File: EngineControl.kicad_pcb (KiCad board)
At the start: 4 copper layers, 70 x 70 mm, 47 parts, among them J1 Debugger, J2 Centroid, J3 BATT, J5 UART, J7 GPIO, Q1 Q_NMOS_GSD, Q2 Q_NMOS_GSD, SW1 BOOT, U1 STM32F103C8Tx, U2 SN65HVD230, U3 AMS1117-3.3, U4 CPC1135N, Y1 8 Mhz 5032

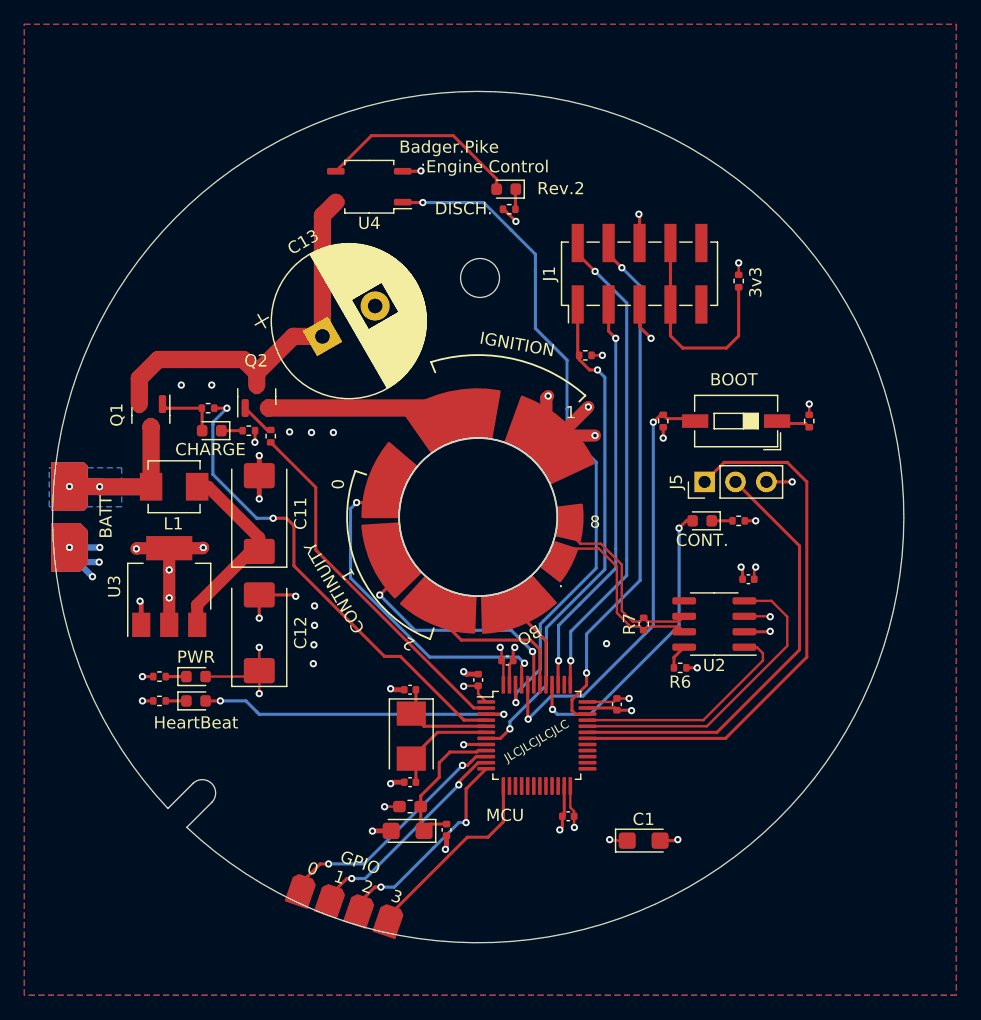
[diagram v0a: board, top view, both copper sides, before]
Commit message: Apply schematic updates to PCB
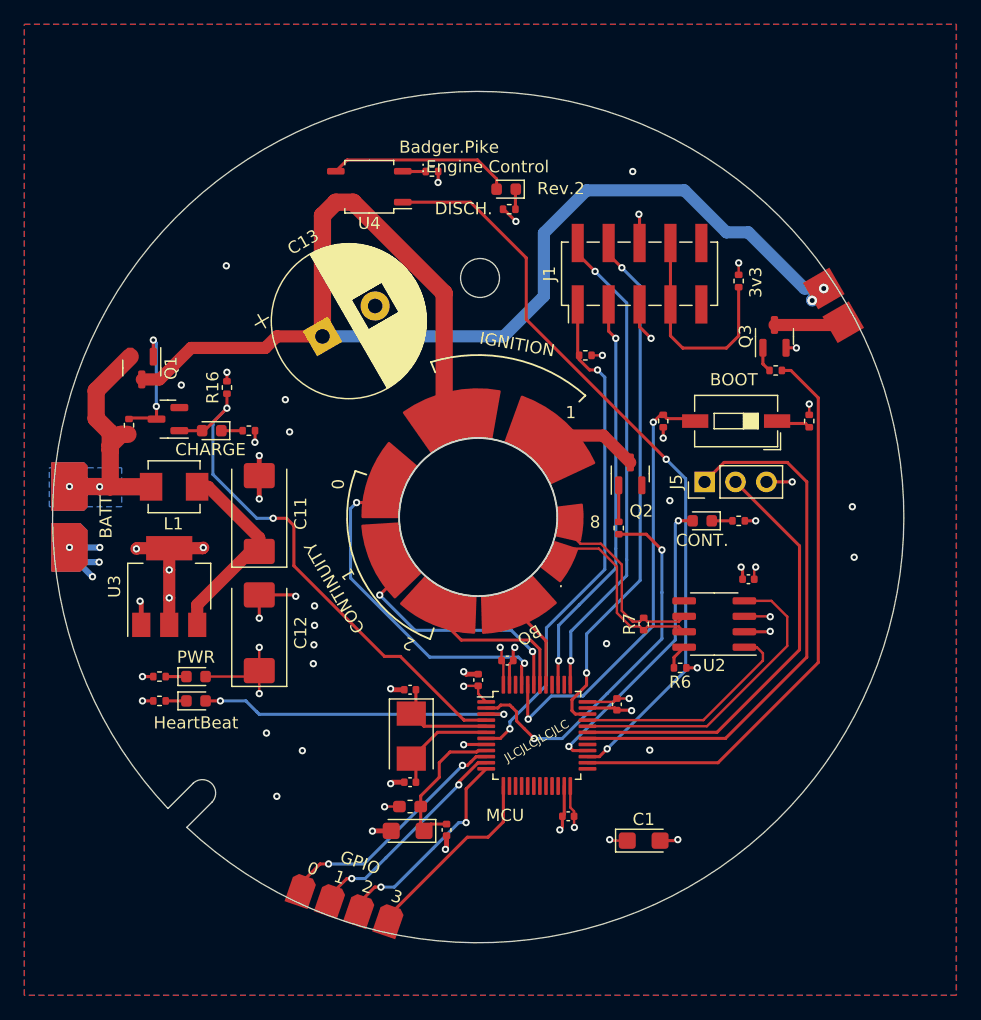
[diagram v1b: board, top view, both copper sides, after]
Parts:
- added J4: PYRO1, Connector_PinHeader_2.54mm:PinHeader_1x02_P2.54mm_Vertical_SMD_Pin1Left, F.Cu at (129.2, 82.6)
- added Q3: Q_NMOS_GSD, Package_TO_SOT_SMD:SOT-23, F.Cu at (124.3, 85.2)
- added Q4: Q_NMOS_GSD, Package_TO_SOT_SMD:SOT-23, F.Cu at (74.5, 92.0)
- added R14: 1.5k, Resistor_SMD:R_0402_1005Metric, F.Cu at (96.2, 71.6)
- added R15: 220R, Resistor_SMD:R_0402_1005Metric, F.Cu at (124.5, 88.0)
- added R16: 10k, Resistor_SMD:R_0402_1005Metric, F.Cu at (79.3, 89.4)
- Q1: value Q_NMOS_GSD -> PMOS-GSD
- R11: value 220R -> 100k
- R9: value 1.5k -> 220
- moved Q2 31.3 mm to (112.5, 96.5)
- moved R13 29.6 mm to (111.5, 100.9)
- moved R11 6.65 mm to (71.3, 92.5), turned to -90 degrees
- moved Q1 3.97 mm to (72.3, 87.8)
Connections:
- C13 pad 1: Net-(C13-Pad1) -> /Ignition/IGN+
- D4 pad 2: Net-(D4-Pad2) -> /Ignition/CHARGE
- J2 pad 1: GND -> /Ignition/IGN-
- Q1 pad 1: Net-(D4-Pad2) -> Net-(Q1-Pad1)
- Q1 pad 2: Net-(C13-Pad1) -> /Ignition/BATT+
- Q1 pad 3: /Ignition/BATT+ -> /Ignition/IGN+
- Q2 pad 2: /Ignition/IGN+ -> GND
- Q2 pad 3: Net-(C13-Pad1) -> /Ignition/IGN-
- R11 pad 1: /Ignition/CHARGE -> Net-(Q1-Pad1)
- R11 pad 2: Net-(D4-Pad2) -> /Ignition/BATT+
- U1 pad 26: unconnected-(U1-Pad26) -> /Ignition/IGN1
- U1 pad 27: unconnected-(U1-Pad27) -> /Ignition/nDISCHARGE
- U1 pad 28: unconnected-(U1-Pad28) -> /Ignition/CONT_INDICATION
- U1 pad 40: /Ignition/CONT_INDICATION -> unconnected-(U1-Pad40)
- U1 pad 46: /Ignition/nDISCHARGE -> unconnected-(U1-Pad46)
- U4 pad 2: GND -> Net-(U4-Pad2)
- U4 pad 4: Net-(C13-Pad1) -> /Ignition/IGN+
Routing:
- net /Ignition/IGN+: track 15.6 -> 104.3 mm, vias 0 -> 2
- net /Ignition/IGN1: track 0.00 -> 48.1 mm
- net Net-(C13-Pad1): track 32.0 -> 0.00 mm
- net GND: track 71.4 -> 59.8 mm, vias 45 -> 51
- net Net-(Q1-Pad1): track 0.00 -> 10.3 mm, vias 0 -> 2
- net /Ignition/BATT+: track 11.6 -> 21.5 mm
- net /Ignition/IGN-: track 0.00 -> 8.02 mm
- net /Ignition/nDISCHARGE: track 55.8 -> 62.4 mm
- net /Ignition/PYRO1-: track 0.00 -> 5.74 mm
- net Net-(D4-Pad2): track 5.24 -> 0.00 mm
- net /Ignition/CHARGE: track 39.7 -> 44.5 mm
- net Net-(Q3-Pad1): track 0.00 -> 2.09 mm
- net Net-(U4-Pad2): track 0.00 -> 1.90 mm
- net Net-(D5-Pad2): track 16.7 -> 15.1 mm
- net /Ignition/IGN0: track 29.8 -> 30.9 mm, vias 0 -> 2

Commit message: Bump to Rev.3
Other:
- board text added: "Rev.3"
- board text removed: "Rev.2"
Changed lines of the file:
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@@
     (effects (font (size 1 1) (thickness 0.15)))
   )
-  (gr_text "Rev.2" (at 106.8 73.01) (layer "F.SilkS")
+  (gr_text "Rev.3" (at 106.8 73.01) (layer "F.SilkS")
     (effects (font (size 1 1) (thickness 0.15)))
   )

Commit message: Bump version to Rev4 for next release
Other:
- board text added: "PYRO1"
- board text added: "Rev.4"
- board text removed: "Rev.3"
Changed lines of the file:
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@@
+    (effects (font (size 1 1) (thickness 0.15)))
+  )
+  (gr_text "PYRO1" (at 126.85 83.96 120) (layer "F.SilkS")
     (effects (font (size 1 1) (thickness 0.15)))
   )
@@
     (effects (font (size 1 1) (thickness 0.15)))
   )
-  (gr_text "Rev.3" (at 106.8 73.01) (layer "F.SilkS")
+  (gr_text "Rev.4" (at 106.8 73.01) (layer "F.SilkS")
     (effects (font (size 1 1) (thickness 0.15)))
   )

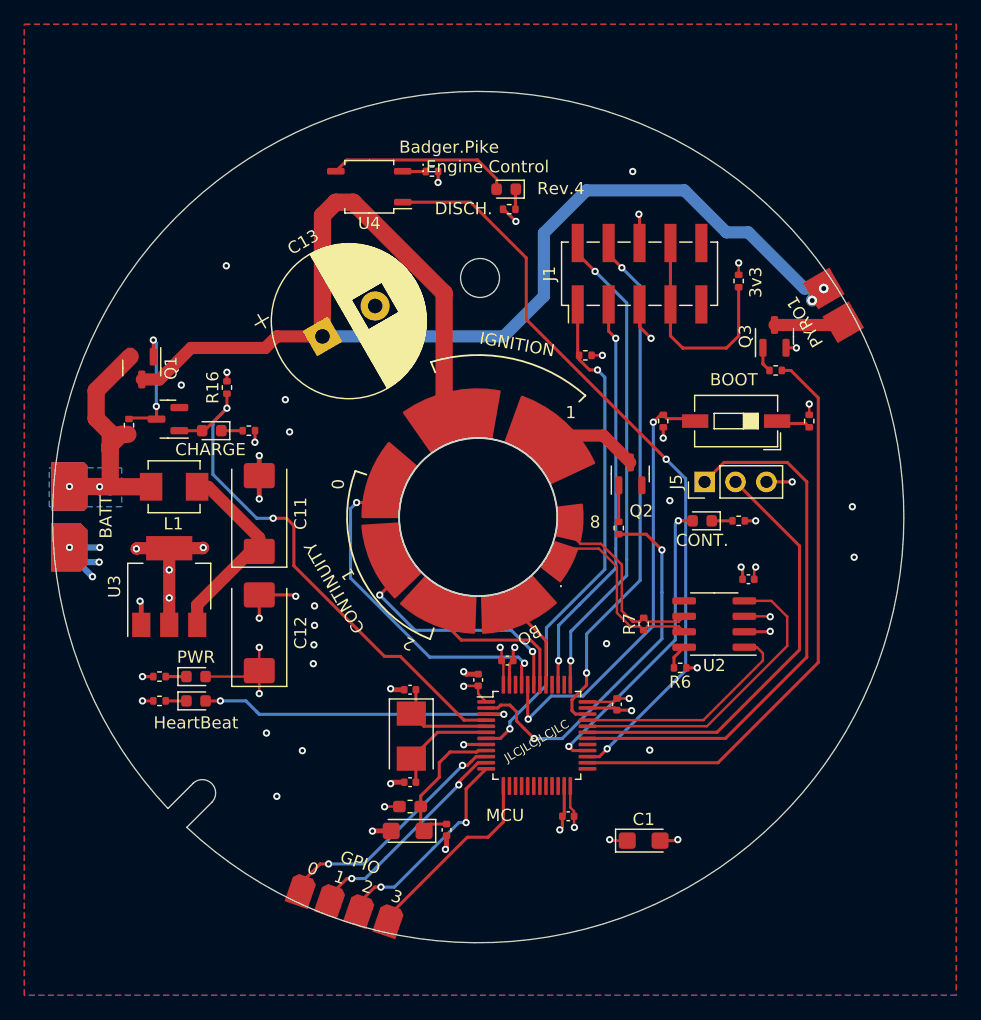
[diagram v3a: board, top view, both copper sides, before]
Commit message: Add pressure sensor schema and pcb layout for pyro and reverse polarity
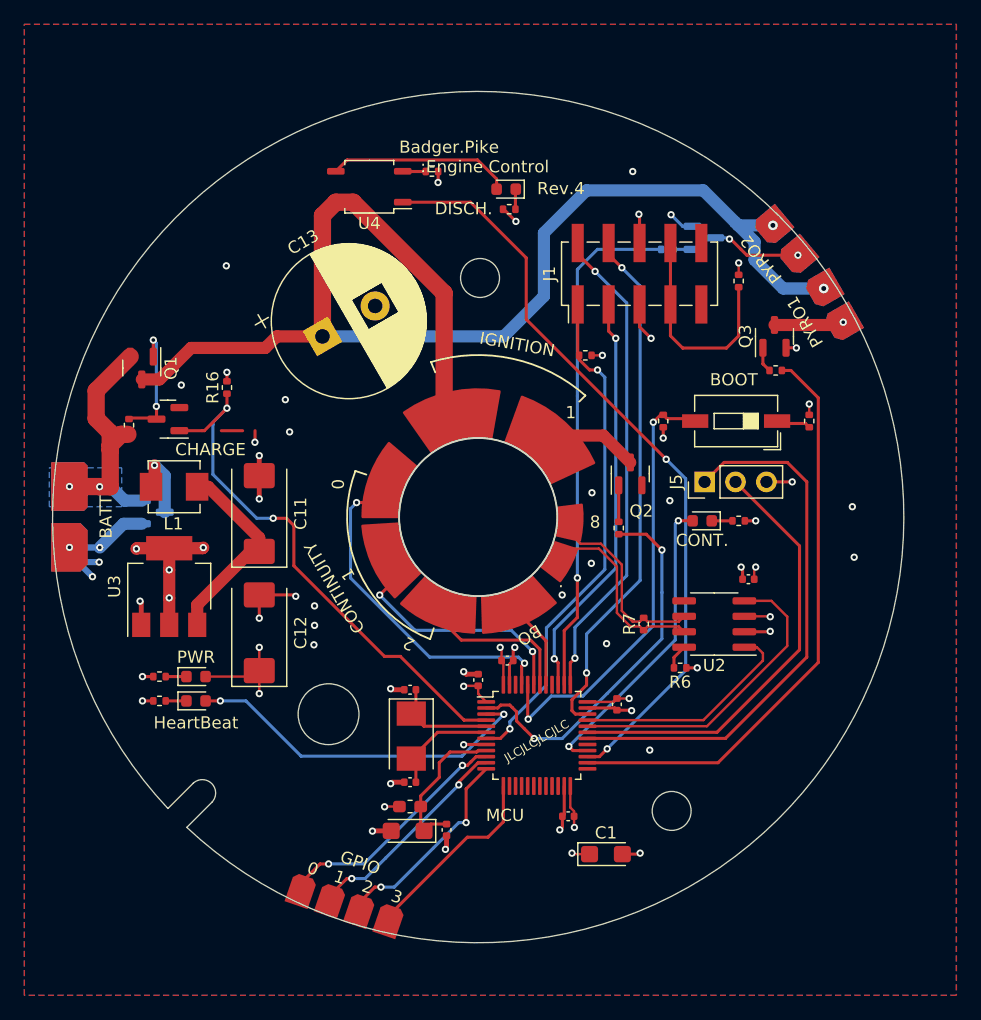
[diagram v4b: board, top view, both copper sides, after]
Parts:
- removed D4: LED_Charge, LED_SMD:LED_0603_1608Metric
- added J6: PYRO2, Connector_PinHeader_2.54mm:PinHeader_1x02_P2.54mm_Vertical_SMD_Pin1Left, F.Cu at (125.2, 77.3)
- added Q5: PMOS-GSD, Package_TO_SOT_SMD:SOT-23, B.Cu at (73.3, 99.6)
- added Q6: Q_NMOS_GSD, Package_TO_SOT_SMD:SOT-23, B.Cu at (118.5, 77.1)
- added REF**: MountingHole_5mm, MountingHole:MountingHole_5mm, F.Cu at (87.7, 116.2)
- added REF**: MountingHole_3.2mm_M3, MountingHole:MountingHole_3.2mm_M3, F.Cu at (115.9, 124.2)
- C12: value 100u -> 100uF
- R9: value 220 -> 220R; moved to B.Cu
- moved R9 37.5 mm to (115.5, 78.0), turned to 0 degrees
- moved C1 3.29 mm to (110.5, 127.7)
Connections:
- J1 pad 10: unconnected-(J1-Pad10) -> (no net)
- J1 pad 9: unconnected-(J1-Pad9) -> (no net)
- L1 pad 1: /Ignition/BATT+ -> Net-(L1-Pad1)
- R9 pad 1: GND -> /Ignition/IGN2
- U1 pad 14: unconnected-(U1-Pad14) -> (no net)
- U1 pad 15: unconnected-(U1-Pad15) -> (no net)
- U1 pad 16: unconnected-(U1-Pad16) -> (no net)
- U1 pad 17: unconnected-(U1-Pad17) -> (no net)
- U1 pad 18: unconnected-(U1-Pad18) -> (no net)
- U1 pad 19: unconnected-(U1-Pad19) -> (no net)
- U1 pad 20: unconnected-(U1-Pad20) -> (no net)
- U1 pad 21: /MCU/SCL -> (no net)
- U1 pad 22: /MCU/SDA -> (no net)
- U1 pad 25: unconnected-(U1-Pad25) -> (no net)
- U1 pad 29: unconnected-(U1-Pad29) -> (no net)
- U1 pad 38: unconnected-(U1-Pad38) -> /Ignition/IGN2
- U1 pad 40: unconnected-(U1-Pad40) -> (no net)
- U1 pad 46: unconnected-(U1-Pad46) -> (no net)
- U2 pad 5: unconnected-(U2-Pad5) -> (no net)
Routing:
- net /Ignition/IGN2: track 0.00 -> 42.1 mm, vias 0 -> 1
- net /Ignition/PYRO2-: track 0.00 -> 7.38 mm, vias 0 -> 2
- net GND: track 59.8 -> 66.2 mm
- net Net-(L1-Pad1): track 0.00 -> 6.07 mm, vias 0 -> 1
- net Net-(D1-Pad2): track 26.4 -> 29.3 mm
- net /Ignition/IGN+: track 104.3 -> 107.0 mm
- net (no net): track 0.00 -> 1.75 mm
- net /Ignition/BATT+: track 21.5 -> 22.0 mm
- net /Ignition/PYRO1-: vias 0 -> 1
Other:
- board text added: "PYRO2"

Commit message: Finish pcb layout for rev4
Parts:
- removed the REF** at (115.9, 124.2)
- added C14: 10uF, Capacitor_Tantalum_SMD:CP_EIA-3216-18_Kemet-A, B.Cu at (122.5, 121.2)
- added C15: 100nF, Capacitor_SMD:C_0402_1005Metric, B.Cu at (120.7, 120.4)
- added C16: 100nF, Capacitor_SMD:C_0402_1005Metric, B.Cu at (120.8, 123.3)
- added R17: 10k, Resistor_SMD:R_0402_1005Metric, F.Cu at (109.2, 122.5)
- added R18: 10k, Resistor_SMD:R_0402_1005Metric, F.Cu at (106.2, 126.8)
- added U5: MPL3115A2, Package_LGA:NXP_LGA-8_3x5mm_P1.25mm_H1.1mm, B.Cu at (116.5, 121.8)
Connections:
- U1 pad 14: (no net) -> /MCU/MPL_INT1
- U1 pad 15: (no net) -> /MCU/MPL_INT2
- U1 pad 21: (no net) -> /MCU/SCL
- U1 pad 22: (no net) -> /MCU/SDA
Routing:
- net /MCU/SCL: track 0.00 -> 16.2 mm, vias 0 -> 1
- net /MCU/MPL_INT1: track 0.00 -> 15.1 mm, vias 0 -> 1
- net /MCU/MPL_INT2: track 0.00 -> 13.8 mm, vias 0 -> 1
- net /MCU/SDA: track 0.00 -> 13.0 mm, vias 0 -> 1
- net +3V3: track 42.0 -> 52.1 mm, vias 17 -> 21
- net Net-(C16-Pad1): track 0.00 -> 3.80 mm
- net GND: track 66.2 -> 69.4 mm, vias 51 -> 53
- net (no net): track 1.75 -> 0.00 mm
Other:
- board text added: "+"
- board text added: "BATT"
- board text removed: "CHARGE"

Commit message: Generate gerber file
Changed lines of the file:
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@@
     (fp_line (start 1.6 0.8) (end -1.2 0.8) (layer "B.Fab") (width 0.1))
     (fp_line (start -1.6 -0.8) (end 1.6 -0.8) (layer "B.Fab") (width 0.1))
-    (pad "1" smd roundrect locked (at -1.35 0 270) (size 1.4 1.35) (layers "B.Cu" "B.Paste" "B.Mask") (roundrect_rratio 0.185185)
+    (pad "1" smd roundrect locked (at -1.35 0 270) (size 1.4 1.35) (layers "B.Cu" "B.Paste" "B.Mask") (roundrect_rratio 0.1851851852)
       (net 1 "+3V3") (pintype "passive"))
-    (pad "2" smd roundrect locked (at 1.35 0 270) (size 1.4 1.35) (layers "B.Cu" "B.Paste" "B.Mask") (roundrect_rratio 0.185185)
+    (pad "2" smd roundrect locked (at 1.35 0 270) (size 1.4 1.35) (layers "B.Cu" "B.Paste" "B.Mask") (roundrect_rratio 0.1851851852)
       (net 2 "GND") (pintype "passive"))
     (model "${KICAD6_3DMODEL_DIR}/Capacitor_Tantalum_SMD.3dshapes/CP_EIA-3216-18_Kemet-A.wrl"
